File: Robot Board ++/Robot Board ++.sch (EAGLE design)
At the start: 119 parts, among them U10 74LVTH125.RGY, U11 SCHA4B0400, U12 BLUETOOTH-RN41", U13 XBEE-1XBEE-1_LOCK, U5 TPS5331[8/9].DQP, U6 TPS62082.DSG, U7 PCA9557.RGV, U8 MPU-6050

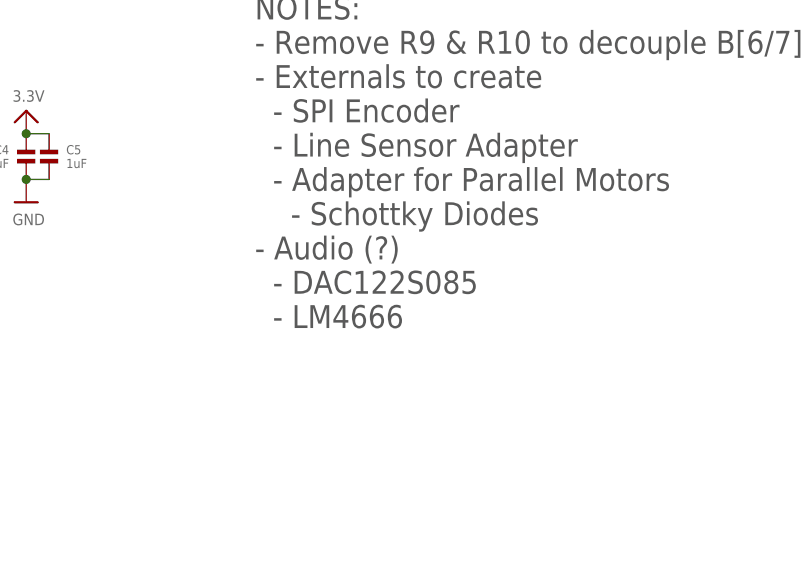
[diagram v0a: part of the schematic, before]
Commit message: Removed ICs for Audio in list of ToDo Minorly adjusted bottom silk screen
Barring any major issues, board will be sent out to be manufactured tomorrow!
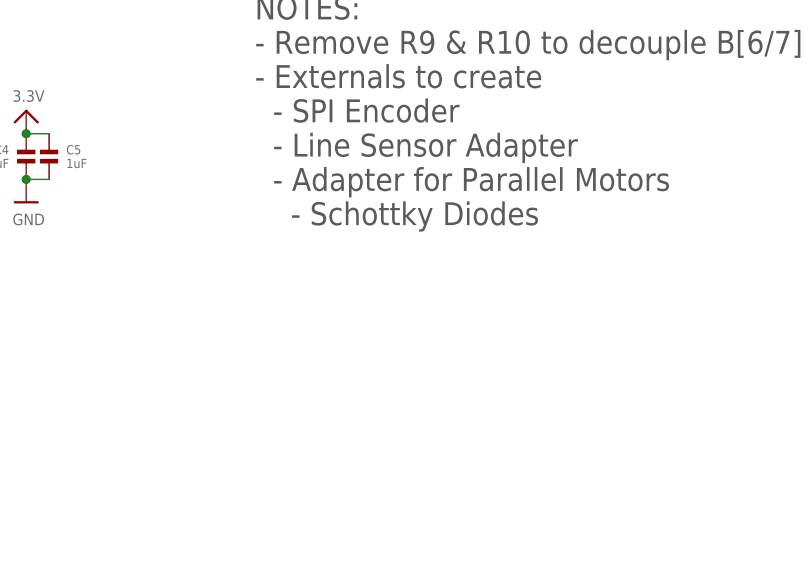
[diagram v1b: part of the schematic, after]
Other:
- note added: "NOTES: - Remove R9 & R10 to decouple B[6/7] from D[0/1] - Externals to create - SPI Encoder - Line Sensor Adapter - Adapter for Parallel Motors - Schottky Diodes"
- note removed: "NOTES: - Remove R9 & R10 to decouple B[6/7] from D[0/1] - Externals to create - SPI Encoder - Line Sensor Adapter - Adapter for Parallel Motors - Schottky Diodes - Audio (?) - DAC122S085 - LM4666"
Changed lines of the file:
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@@
   - Line Sensor Adapter
   - Adapter for Parallel Motors
-    - Schottky Diodes
-- Audio (?)
-  - DAC122S085
-  - LM4666</text>
+    - Schottky Diodes</text>
 </plain>
 <instances>
